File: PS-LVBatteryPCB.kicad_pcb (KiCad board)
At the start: 2 copper layers, 23.4 x 39.8 mm, 10 parts, among them J1 NTC_01, J2 NTC_02, J3 NTC_OUT, J4 SUPP+, J5 SUPP_GND, J6 SUPP_FUSE

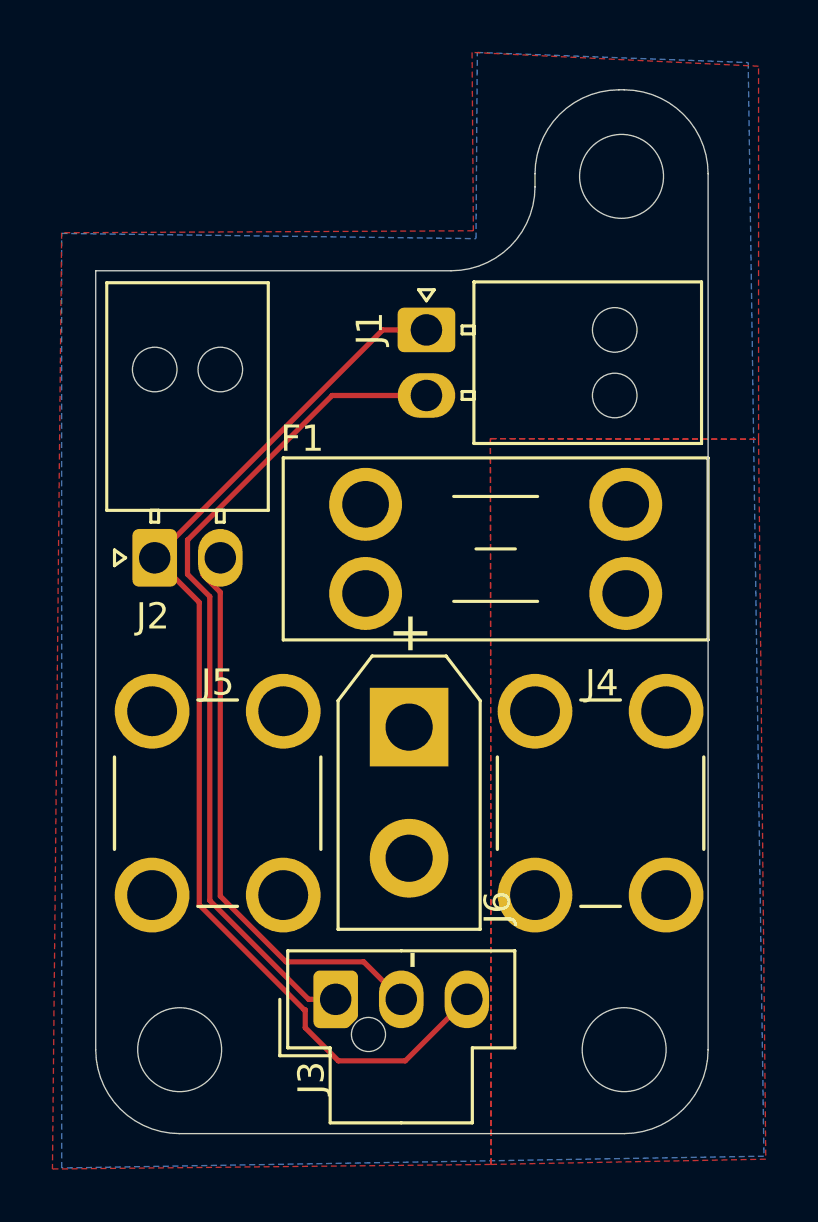
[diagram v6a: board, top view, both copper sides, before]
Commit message: Specified some silkscreen labels + attribution
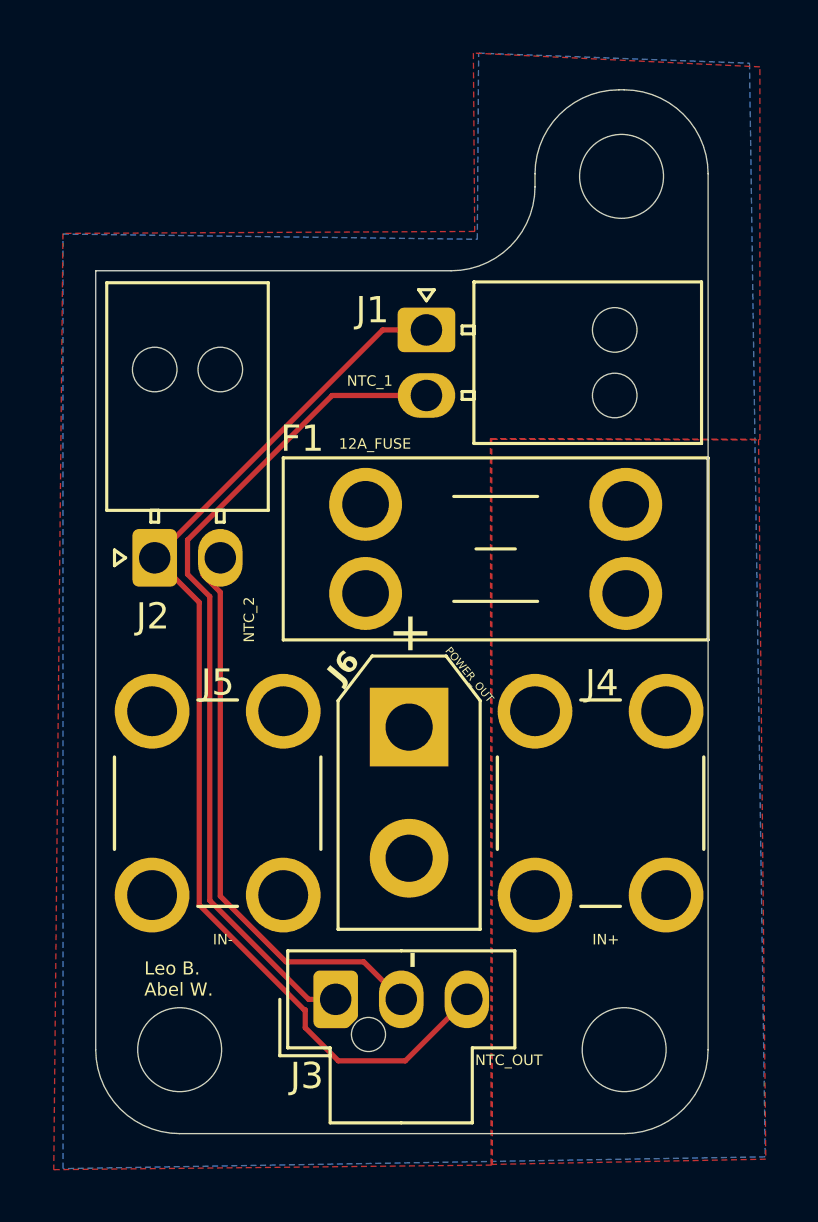
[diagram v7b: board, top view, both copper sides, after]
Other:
- board text added: "12A_FUSE"
- board text added: "IN+"
- board text added: "IN-"
- board text added: "Leo B. Abel W."
- board text added: "NTC_1"
- board text added: "NTC_2"
- board text added: "NTC_OUT"
- board text added: "POWER_OUT"
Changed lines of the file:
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@@
 		(tags "connector Molex Nano-Fit vertical")
 		(property "Reference" "J3"
-			(at -2.995 -0.925 90)
+			(at -2.92 -1.1 0)
 			(layer "F.SilkS")
 			(effects
@@
 		(tags "RC Connector XT30")
 		(property "Reference" "J6"
-			(at 6.875 -3.375 90)
-			(layer "F.SilkS")
-			(effects
-				(font
-					(size 1 1)
-					(thickness 0.15)
+			(at -2.3 2.5 50)
+			(layer "F.SilkS")
+			(effects
+				(font
+					(size 0.8 0.8)
+					(thickness 0.15)
+					(bold yes)
 				)
 			)
@@
 		(tags "connector Molex Nano-Fit horizontal")
 		(property "Reference" "J1"
-			(at -2.16 -0.055 90)
+			(at -2.06 -0.755 0)
 			(layer "F.SilkS")
 			(effects
@@
 		(layer "Edge.Cuts")
 	)
+	(gr_text "IN-"
+		(at 191.3 91.2 0)
+		(layer "F.SilkS")
+		(effects
+			(font
+				(size 0.4 0.4)
+				(thickness 0.075)
+			)
+		)
+	)
+	(gr_text "Leo B.\nAbel W."
+		(at 188.3 93.4 0)
+		(layer "F.SilkS")
+		(effects
+			(font
+				(size 0.5 0.5)
+				(thickness 0.1)
+			)
+			(justify left bottom)
+		)
+	)
+	(gr_text "NTC_2"
+		(at 192.3 79 90)
+		(layer "F.SilkS")
+		(effects
+			(font
+				(size 0.4 0.4)
+				(thickness 0.075)
+			)
+		)
+	)
+	(gr_text "POWER_OUT"
+		(at 200.7 81.1 310)
+		(layer "F.SilkS")
+		(effects
+			(font
+				(size 0.3 0.3)
+				(thickness 0.075)
+			)
+		)
+	)
+	(gr_text "NTC_OUT"
+		(at 202.2 95.8 0)
+		(layer "F.SilkS")
+		(effects
+			(font
+				(size 0.4 0.4)
+				(thickness 0.075)
+			)
+		)
+	)
+	(gr_text "NTC_1"
+		(at 196.9 69.9 0)
+		(layer "F.SilkS")
+		(effects
+			(font
+				(size 0.4 0.4)
+				(thickness 0.075)
+			)
+		)
+	)
+	(gr_text "IN+"
+		(at 205.9 91.2 0)
+		(layer "F.SilkS")
+		(effects
+			(font
+				(size 0.4 0.4)
+				(thickness 0.075)
+			)
+		)
+	)
+	(gr_text "12A_FUSE"
+		(at 197.1 72.3 0)
+		(layer "F.SilkS")
+		(effects
+			(font
+				(size 0.4 0.4)
+				(thickness 0.075)
+			)
+		)
+	)
 	(segment
 		(start 194.439 94.562238)
@@
 		(polygon
 			(pts
-				(xy 201.525 99.775) (xy 201.5 72.1) (xy 211.725 72.125) (xy 211.725 57.9) (xy 200.8 57.375) (xy 200.85 64.175)
-				(xy 185.15 64.25) (xy 184.8 99.95)
+				(xy 201.575 99.8) (xy 201.55 72.125) (xy 211.775 72.15) (xy 211.775 57.925) (xy 200.85 57.4) (xy 200.9 64.2)
+				(xy 185.2 64.275) (xy 184.85 99.975)
 			)
 		)
@@
 		(min_thickness 0.25)
 		(filled_areas_thickness no)
-		(fill yes
+		(fill
 			(thermal_gap 0.5)
 			(thermal_bridge_width 0.5)
@@
 		(polygon
 			(pts
-				(xy 185.15 64.275) (xy 200.95 64.475) (xy 201 57.375) (xy 211.328929 57.760552) (xy 211.928929 99.460552)
-				(xy 185.153929 99.910552)
-			)
-		)
+				(xy 185.2 64.3) (xy 201 64.5) (xy 201.05 57.4) (xy 211.378929 57.785552) (xy 211.978929 99.485552)
+				(xy 185.203929 99.935552)
+			)
+		)

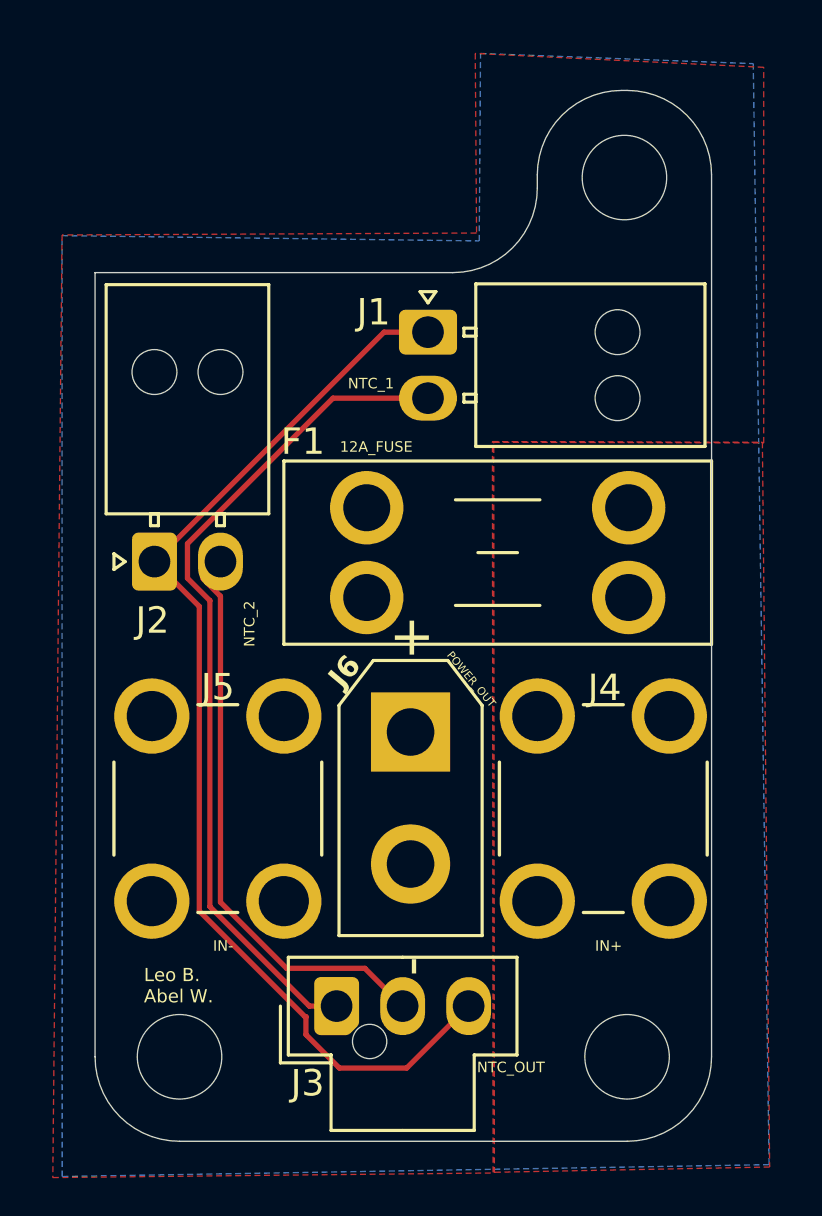
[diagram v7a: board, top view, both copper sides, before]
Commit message: centered top mount, touched up ss
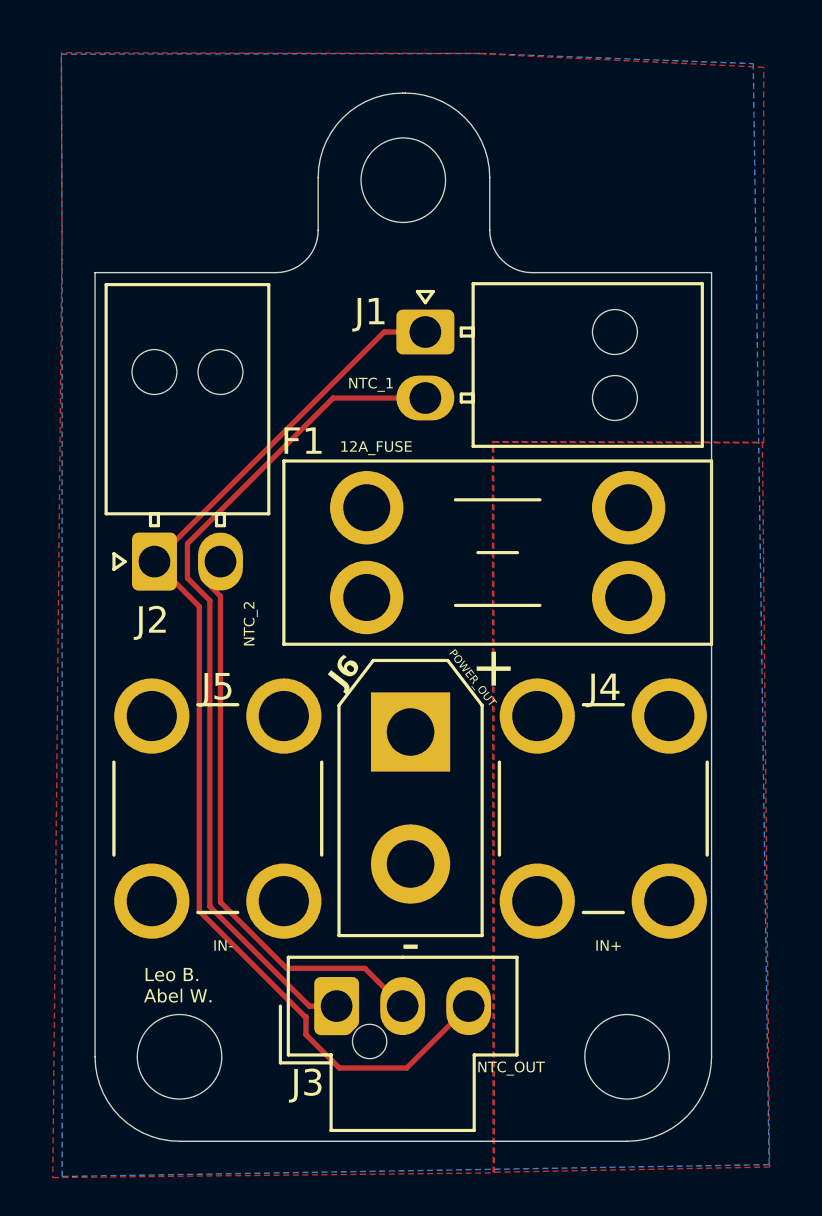
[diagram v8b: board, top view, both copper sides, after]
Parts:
- moved REF** 8.38 mm to (198.1, 62.2)
- moved J1 0.10 mm to (199.0, 68.0)
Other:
- board size 23.4 x 39.8 mm -> 23.4 x 39.7 mm
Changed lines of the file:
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@@
 		(tags "RC Connector XT30")
 		(property "Reference" "J6"
-			(at -2.3 2.5 50)
+			(at -2.3 2.5 52)
 			(layer "F.SilkS")
 			(effects
@@
 		)
 		(fp_text user "+"
-			(at -3.575 0 90)
+			(at -2.4 -3.1 90)
 			(layer "F.SilkS")
 			(effects
@@
 		)
 		(fp_text user "-"
-			(at 8.875 0 90)
+			(at 8 0 180)
 			(layer "F.SilkS")
 			(effects
@@
 	(footprint "Connector_Molex:Molex_Nano-Fit_105313-xx02_1x02_P2.50mm_Horizontal"
 		(layer "F.Cu")
-		(at 199.06 67.955)
+		(at 198.96 67.95)
 		(descr "Molex Nano-Fit Power Connectors, 105313-xx02, 2 Pins per row (http://www.molex.com/pdm_docs/sd/1053131208_sd.pdf), generated with kicad-footprint-generator")
 		(tags "connector Molex Nano-Fit horizontal")
@@
 	(footprint "MountingHole:MountingHole_3.2mm_M3"
 		(layer "F.Cu")
-		(at 206.5 62.1)
+		(at 198.125 62.2)
 		(descr "Mounting Hole 3.2mm, M3, no annular, generated by kicad-footprint-generator mountinghole.py")
 		(tags "mountinghole M3")
@@
 		(embedded_fonts no)
 	)
-	(gr_arc
-		(start 203.2 62.5)
-		(mid 202.262742 64.762742)
-		(end 200 65.7)
+	(gr_line
+		(start 198.1 58.9)
+		(end 198.2 58.9)
 		(stroke
 			(width 0.05)
@@
 	)
 	(gr_line
-		(start 209.8 62)
-		(end 209.8 95.4)
+		(start 201.4 62.1)
+		(end 201.4 64.1)
 		(stroke
 			(width 0.05)
@@
 		(layer "Edge.Cuts")
 	)
-	(gr_line
-		(start 186.45 65.7)
-		(end 200 65.7)
+	(gr_arc
+		(start 203 65.7)
+		(mid 201.868629 65.231371)
+		(end 201.4 64.1)
 		(stroke
 			(width 0.05)
@@
 	)
 	(gr_arc
-		(start 206.6 58.8)
-		(mid 208.862742 59.737258)
-		(end 209.8 62)
+		(start 194.9 62.1)
+		(mid 195.837258 59.837258)
+		(end 198.1 58.9)
+		(stroke
+			(width 0.05)
+			(type default)
+		)
+		(layer "Edge.Cuts")
+	)
+	(gr_line
+		(start 194.9 64.1)
+		(end 194.9 62.1)
+		(stroke
+			(width 0.05)
+			(type default)
+		)
+		(layer "Edge.Cuts")
+	)
+	(gr_line
+		(start 203 65.7)
+		(end 209.8 65.7)
+		(stroke
+			(width 0.05)
+			(type default)
+		)
+		(layer "Edge.Cuts")
+	)
+	(gr_line
+		(start 186.45 65.7)
+		(end 193.3 65.7)
+		(stroke
+			(width 0.05)
+			(type default)
+		)
+		(layer "Edge.Cuts")
+	)
+	(gr_arc
+		(start 198.2 58.9)
+		(mid 200.462742 59.837258)
+		(end 201.4 62.1)
 		(stroke
 			(width 0.05)
@@
 		(layer "Edge.Cuts")
 	)
-	(gr_line
-		(start 203.2 62.5)
-		(end 203.2 62)
-		(stroke
-			(width 0.05)
-			(type default)
-		)
-		(layer "Edge.Cuts")
-	)
 	(gr_arc
 		(start 189.65 98.6)
@@
 		(layer "Edge.Cuts")
 	)
+	(gr_arc
+		(start 194.9 64.1)
+		(mid 194.431371 65.231371)
+		(end 193.3 65.7)
+		(stroke
+			(width 0.05)
+			(type default)
+		)
+		(layer "Edge.Cuts")
+	)
 	(gr_line
-		(start 206.4 58.8)
-		(end 206.6 58.8)
+		(start 209.8 65.7)
+		(end 209.8 95.4)
 		(stroke
 			(width 0.05)
@@
 		(start 186.45 95.4)
 		(end 186.45 65.7)
-		(stroke
-			(width 0.05)
-			(type default)
-		)
-		(layer "Edge.Cuts")
-	)
-	(gr_arc
-		(start 203.2 62)
-		(mid 204.137258 59.737258)
-		(end 206.4 58.8)
 		(stroke
 			(width 0.05)
@@
 	)
 	(gr_text "POWER_OUT"
-		(at 200.7 81.1 310)
+		(at 200.75 81.05 308)
 		(layer "F.SilkS")
 		(effects
@@
 	)
 	(segment
-		(start 199.06 67.955)
-		(end 197.395 67.955)
-		(width 0.2)
-		(layer "F.Cu")
-		(net 3)
-	)
-	(segment
 		(start 194.400867 93.881)
 		(end 190.398 89.878133)
@@
 	)
 	(segment
-		(start 197.395 67.955)
-		(end 188.705 76.645)
-		(width 0.2)
-		(layer "F.Cu")
-		(net 3)
-	)
-	(segment
 		(start 195.701762 95.825)
 		(end 194.439 94.562238)
@@
 	(segment
 		(start 188.705 76.645)
-		(end 188.7 76.645)
+		(end 197.4 67.95)
 		(width 0.2)
 		(layer "F.Cu")
@@
 	)
 	(segment
-		(start 190.799 78.12176)
-		(end 189.95 77.27276)
+		(start 197.4 67.95)
+		(end 198.96 67.95)
 		(width 0.2)
 		(layer "F.Cu")
+		(net 3)
+	)
+	(segment
+		(start 188.7 76.645)
+		(end 188.705 76.645)
+		(width 0.2)
+		(layer "F.Cu")
+		(net 3)
+	)
+	(segment
+		(start 195.6 93.48)
+		(end 194.566967 93.48)
+		(width 0.2)
+		(layer "F.Cu")
 		(net 4)
 	)
 	(segment
-		(start 189.95 75.9671)
-		(end 195.4621 70.455)
+		(start 189.95 77.27276)
+		(end 189.95 75.9671)
 		(width 0.2)
 		(layer "F.Cu")
@@
 	)
 	(segment
-		(start 195.6 93.48)
-		(end 194.566967 93.48)
+		(start 195.4671 70.45)
+		(end 198.96 70.45)
 		(width 0.2)
 		(layer "F.Cu")
@@
 	)
 	(segment
-		(start 189.95 77.27276)
-		(end 189.95 75.9671)
+		(start 189.95 75.9671)
+		(end 195.4671 70.45)
 		(width 0.2)
 		(layer "F.Cu")
@@
 	)
 	(segment
-		(start 195.4621 70.455)
-		(end 199.06 70.455)
+		(start 190.799 78.12176)
+		(end 189.95 77.27276)
 		(width 0.2)
 		(layer "F.Cu")
@@
 		(polygon
 			(pts
-				(xy 201.575 99.8) (xy 201.55 72.125) (xy 211.775 72.15) (xy 211.775 57.925) (xy 200.85 57.4) (xy 200.9 64.2)
+				(xy 201.575 99.8) (xy 201.55 72.125) (xy 211.775 72.15) (xy 211.775 57.925) (xy 200.85 57.4) (xy 185.175 57.375)
 				(xy 185.2 64.275) (xy 184.85 99.975)
 			)
@@
 		(min_thickness 0.25)
 		(filled_areas_thickness no)
-		(fill
+		(fill yes
 			(thermal_gap 0.5)
 			(thermal_bridge_width 0.5)
@@
 		(polygon
 			(pts
-				(xy 185.2 64.3) (xy 201 64.5) (xy 201.05 57.4) (xy 211.378929 57.785552) (xy 211.978929 99.485552)
+				(xy 185.2 64.3) (xy 185.175 57.425) (xy 201.05 57.4) (xy 211.378929 57.785552) (xy 211.978929 99.485552)
 				(xy 185.203929 99.935552)
 			)
